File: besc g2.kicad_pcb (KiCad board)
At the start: 4 copper layers, 231 x 67 mm, 302 parts, among them IC1 LTC7801, J1 PHASE WIRE, J10 614105150721, J11 THROTTLE, J12 MOTOR SENSOR, J13 THROTTLE 2 (BRAKE), J14 SERIAL, J15 IGNITION, J16 CAN, J17 12V OUT, J2 PHASE WIRE, J3 PHASE WIRE, J4 BUSBAR, J5 BUSBAR, J6 IN+, J7 IN-, J8 SWD, J9 RC PWM, Q1 IRF135B203, Q10 IRF135B203, Q11 IRF135B203, Q12 IRF135B203, Q13 IRF135B203, Q14 IRF135B203, Q15 IRF135B203, Q16 IRF135B203, Q17 IRF135B203, Q18 IRF135B203, Q19 IRF135B203, Q2 IRF135B203, Q20 IRF135B203, Q21 IRF135B203, Q22 IRF135B203, Q23 IRF135B203, Q24 IRF135B203, Q25 FDMS86252L, Q26 BSC110N15NS5, Q3 IRF135B203, Q4 IRF135B203, Q5 IRF135B203, Q6 IRF135B203, Q7 IRF135B203, Q8 IRF135B203, Q9 IRF135B203, U1 UCC21520DW, U10 TJA1051T-3, U11 R-78E5.0-0.5, U12 LP5907MFX-3.3, U2 UCC21520DW, U3 UCC21520DW, U4 INA240A1D, U5 INA240A1D, U6 INA240A1D, U7 SN74LVC1G04, U8 STM32F405RGTx, U9 USBLC6-2SC6, Y1 MCSJK-7I-8.00-18-10-60-B-10

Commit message: Fix component label
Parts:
- C66: value 270p -> 2k2
- R66: value 2k2 -> 270p

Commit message: u7 bug fixes
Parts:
- removed U7: SN74LVC1G04, Package_TO_SOT_SMD:SOT-23-5
- renumbered R66 to C66, C66 to R66
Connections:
- J10 pad 4: (no net) -> Net-(J10-Pad4)
- U1 pad 12: (no net) -> Net-(U1-Pad12)
- U1 pad 13: (no net) -> Net-(U1-Pad13)
- U1 pad 7: (no net) -> Net-(U1-Pad7)
- U2 pad 12: (no net) -> Net-(U2-Pad12)
- U2 pad 13: (no net) -> Net-(U2-Pad13)
- U2 pad 7: (no net) -> Net-(U2-Pad7)
- U3 pad 12: (no net) -> Net-(U3-Pad12)
- U3 pad 13: (no net) -> Net-(U3-Pad13)
- U3 pad 7: (no net) -> Net-(U3-Pad7)
- U8 pad 2: (no net) -> Net-(U8-Pad2)
- U8 pad 25: (no net) -> /mcu/ADC15
- U8 pad 28: (no net) -> Net-(U8-Pad28)
- U8 pad 3: (no net) -> Net-(U8-Pad3)
- U8 pad 33: (no net) -> Net-(U8-Pad33)
- U8 pad 4: (no net) -> Net-(U8-Pad4)
- U8 pad 40: (no net) -> Net-(U8-Pad40)
- U8 pad 50: (no net) -> Net-(U8-Pad50)
- U8 pad 51: (no net) -> Net-(U8-Pad51)
- U8 pad 52: (no net) -> Net-(U8-Pad52)
- U8 pad 53: (no net) -> Net-(U8-Pad53)
- U8 pad 54: (no net) -> Net-(U8-Pad54)
- U8 pad 55: (no net) -> Net-(U8-Pad55)
- U8 pad 56: (no net) -> Net-(U8-Pad56)
- U8 pad 57: /mcu/GATE_ENABLE -> /mcu/DISABLE
- U8 pad 59: (no net) -> /mcu/FAULT
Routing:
- net /mcu/GATE_ENABLE: track 31.6 -> 0.00 mm, vias 2 -> 0
- net /mcu/DISABLE: track 156.3 -> 185.4 mm, vias 5 -> 7
- net VDC: track 40.1 -> 53.9 mm
- net GND: track 213.3 -> 215.3 mm
- net +3V3: track 121.3 -> 119.5 mm
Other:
- board text added: "TRAVERSE VESC ryder v0.1"
- board text removed: "TRAVERSE VESC a0.1"

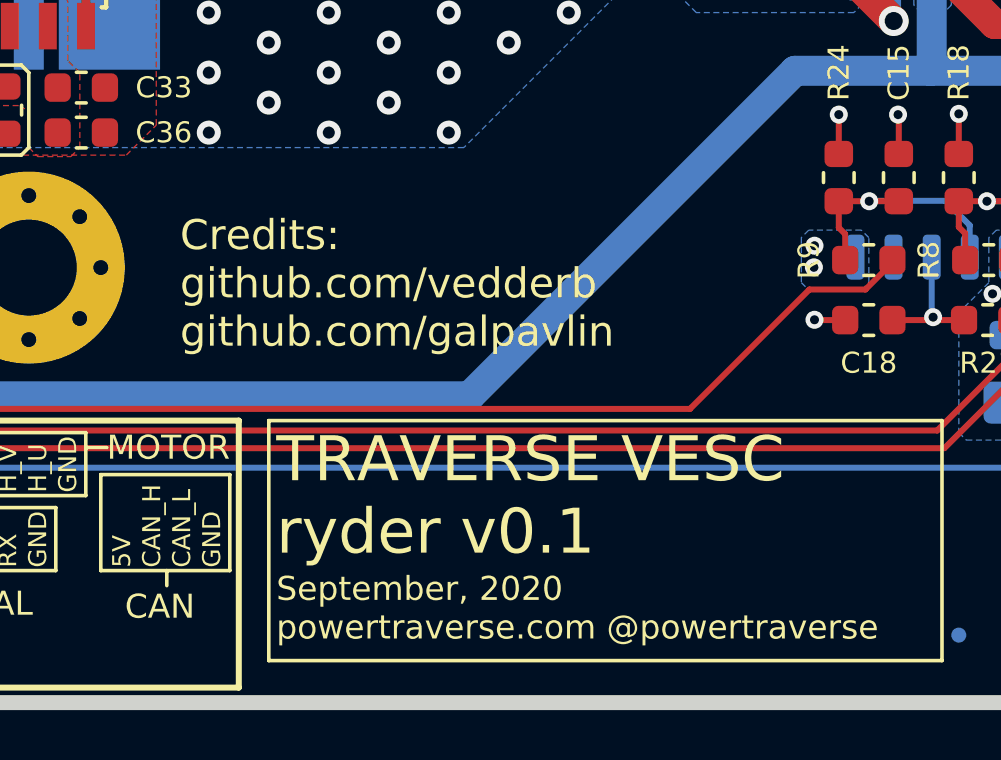
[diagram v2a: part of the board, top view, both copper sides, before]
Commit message: edit silkscreen label
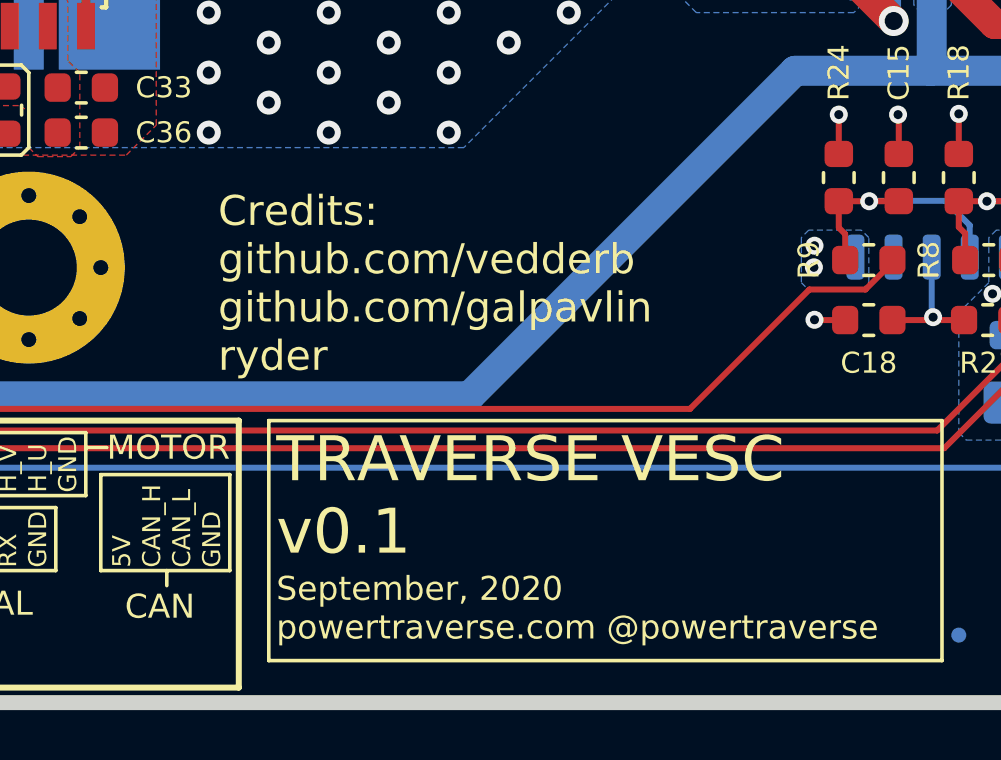
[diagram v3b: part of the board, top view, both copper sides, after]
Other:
- board text added: "Credits: github.com/vedderb github.com/galpavlin ryder"
- board text added: "TRAVERSE VESC v0.1"
- board text removed: "Credits: github.com/vedderb github.com/galpavlin"
- board text removed: "TRAVERSE VESC ryder v0.1"

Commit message: BOM Gerber updates
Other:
- board text added: "Credits: github.com/vedderb github.com/galpavlin Ryder"
- board text removed: "Credits: github.com/vedderb github.com/galpavlin ryder"

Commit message: Nikolay Sirkiza
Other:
- board text added: "Credits: github.com/vedderb github.com/galpavlin"
- board text added: "TRAVERSE VESC a0.1"
- board text removed: "Credits: github.com/vedderb github.com/galpavlin Ryder"
- board text removed: "TRAVERSE VESC v0.1"
